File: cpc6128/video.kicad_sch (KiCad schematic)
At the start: 18 parts, among them J101 MONITOR, Q102 2SC1815Y

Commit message: Update title blocks
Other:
- company: (none) -> Amstrad plc
- title: (none) -> CPC6128 MC0020x Monitor output
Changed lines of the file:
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@@
 (kicad_sch (version 20211123) (generator eeschema)
   (paper "A4")
+  (title_block
+    (title "CPC6128 MC0020x Monitor output")
+    (date "2022-08-20")
+    (rev "1")
+    (company "Amstrad plc")
+  )
   (junction (at 143.51 105.41) (diameter 0) (color 0 0 0 0)
   )

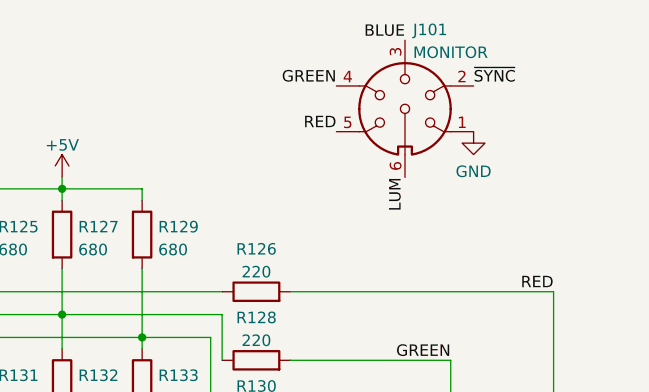
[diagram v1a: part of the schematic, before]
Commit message: Correct C136 (missing) and C314 (wrong footprint) Thanks @orzel!
Also migrated to KiCad 9.
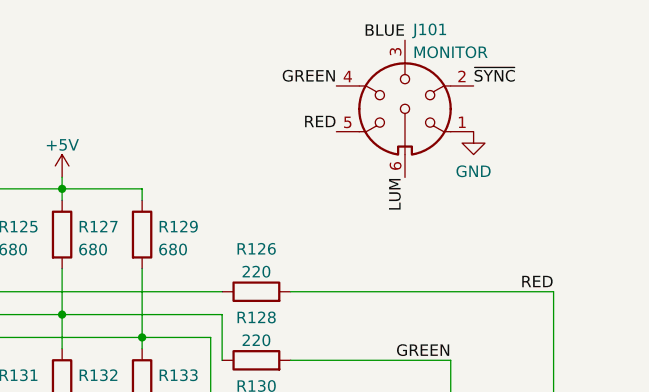
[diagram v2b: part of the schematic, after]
